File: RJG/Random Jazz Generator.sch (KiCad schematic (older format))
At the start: 19 parts, among them J101 EuroPower, J102 CV, J103 RND, J104 Gate, J105 Trig1, J106 Trig2, J107 Clock, J108 Trig3, J109 Trig4, U101 4520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

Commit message: Small improvements
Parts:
- added C101: 10u, symbol Device:CP
- added C102: 1u, symbol Device:CP
- added C103, C104: 100n, Capacitor_THT:C_Disc_D7.0mm_W2.5mm_P5.00mm, symbol Device:C
- renumbered U102 to U101, U101 to U102
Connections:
- net +12V: now also C101.1
- net +5V: now also C102.1, C103.2, C104.2
- net GND: now also C101.2, C102.2, C103.1, C104.1
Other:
- moved on the sheet: U101, U102C

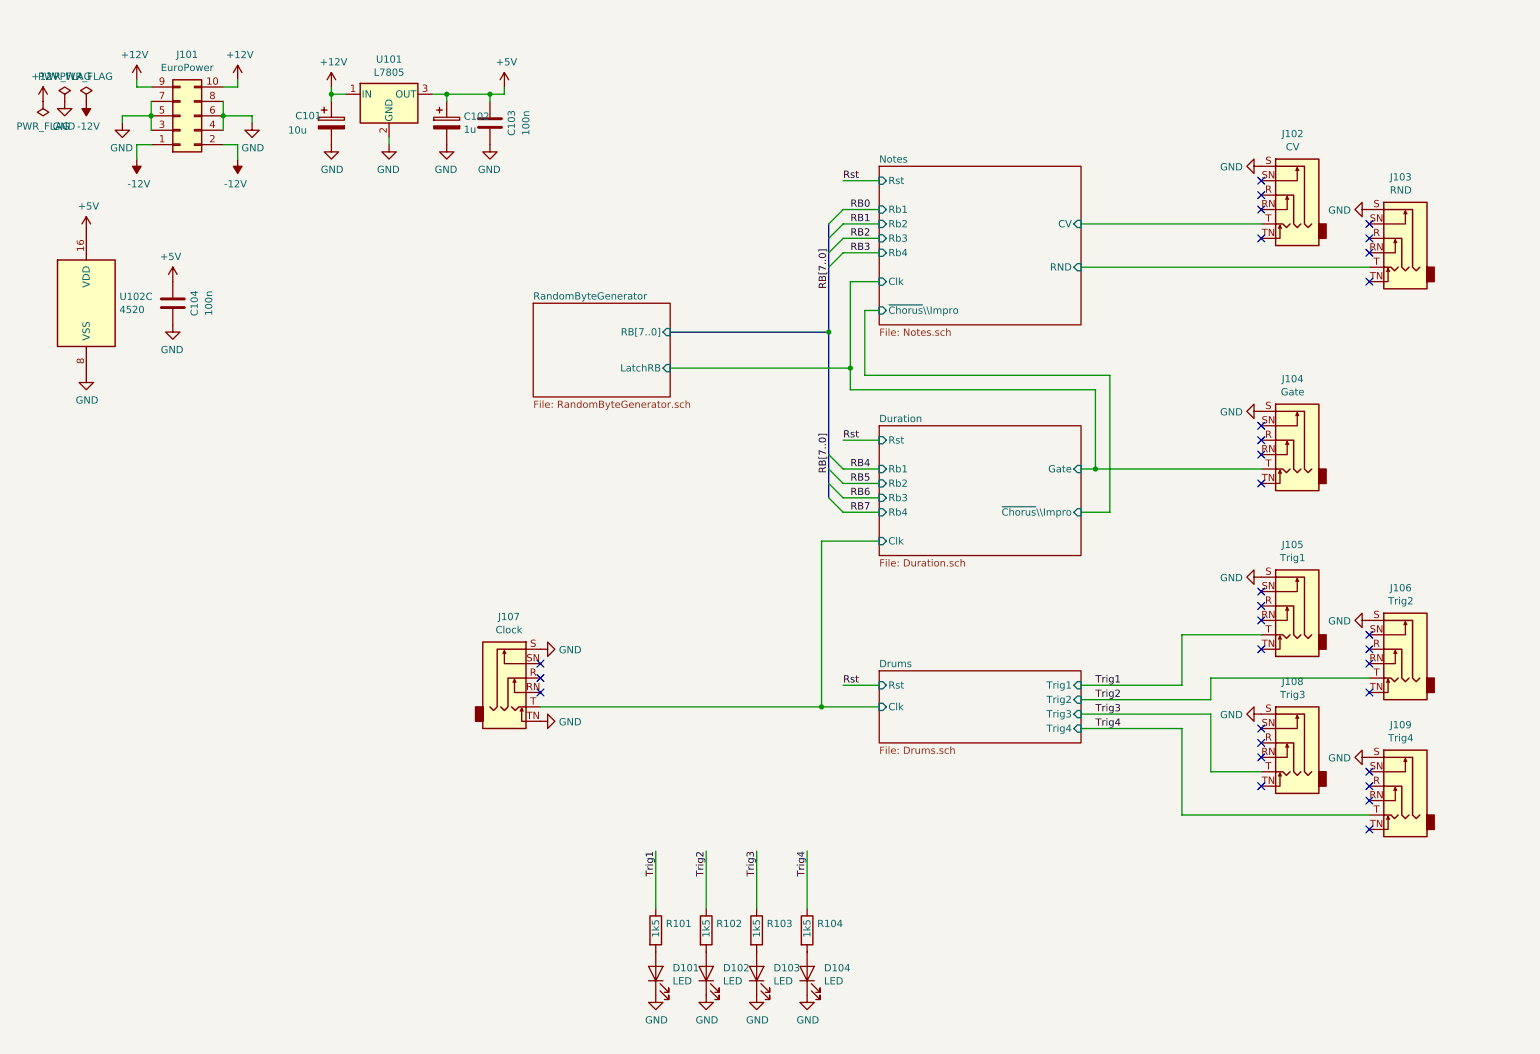
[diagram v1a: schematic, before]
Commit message: Schematic done
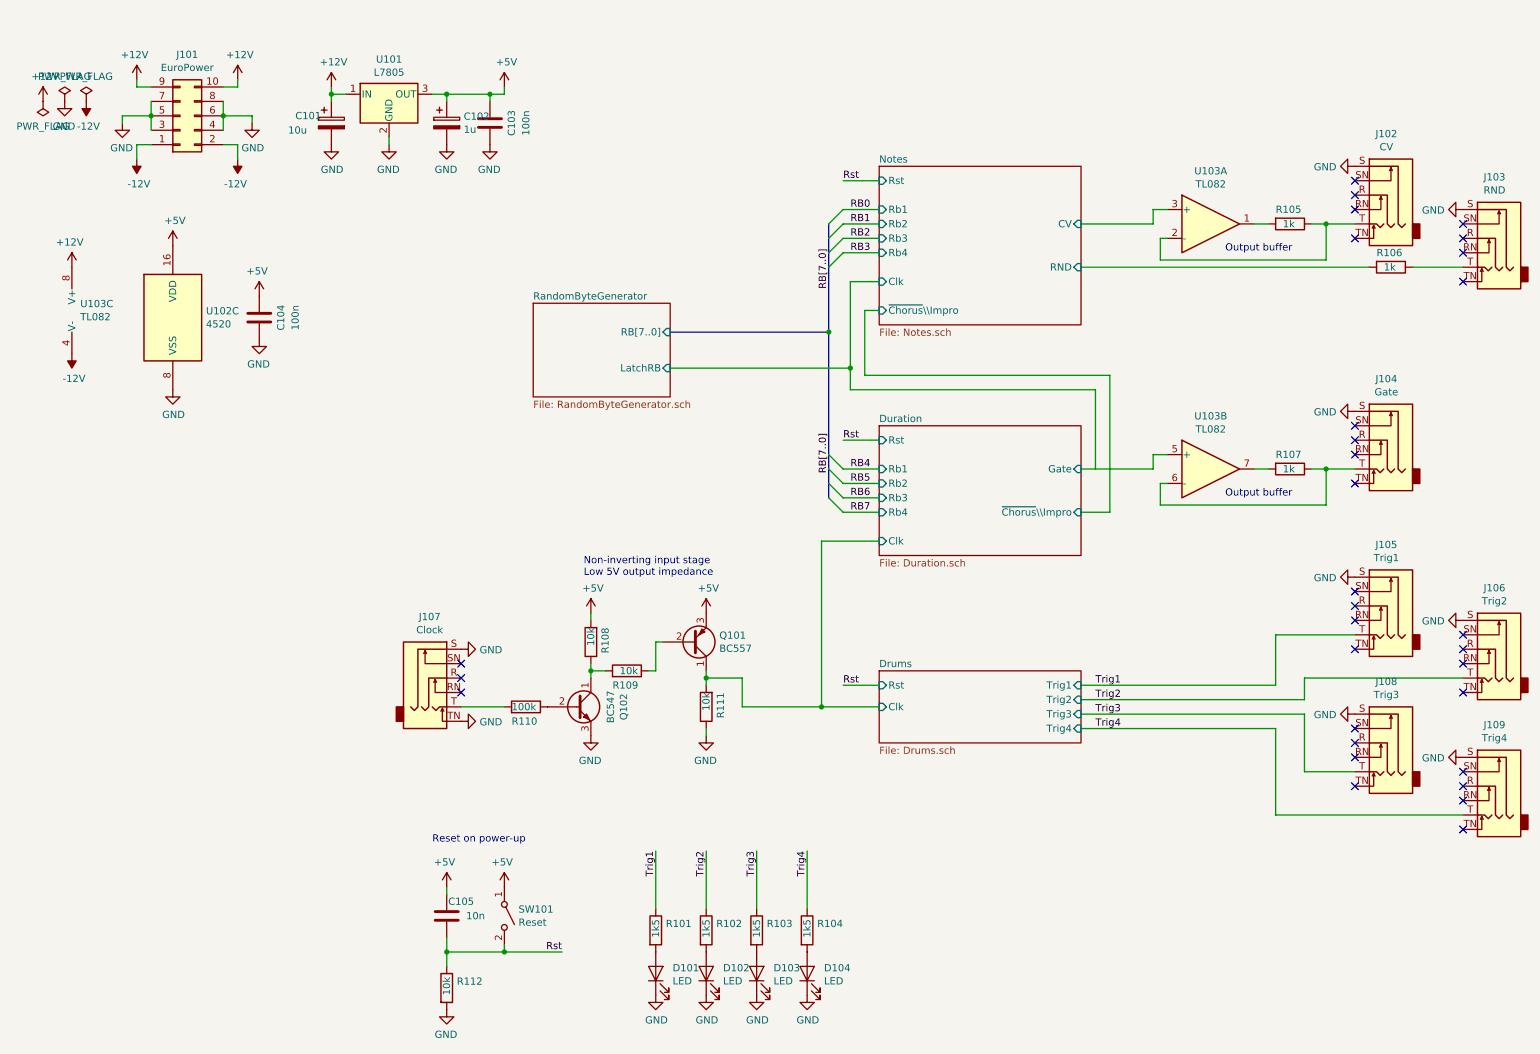
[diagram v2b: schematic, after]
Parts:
- added C105: 10n, Capacitor_THT:C_Disc_D7.0mm_W2.5mm_P5.00mm, symbol Device:C
- added Q101: BC557, Package_TO_SOT_THT:TO-92_Inline_Wide, symbol Transistor_BJT:BC557
- added Q102: BC547, Package_TO_SOT_THT:TO-92_Inline_Wide, symbol Transistor_BJT:BC547
- added R105, R106, R107: 1k, Resistor_THT:R_Axial_DIN0204_L3.6mm_D1.6mm_P7.62mm_Horizontal, symbol Device:R
- added R108, R109, R111, R112: 10k, Resistor_THT:R_Axial_DIN0204_L3.6mm_D1.6mm_P7.62mm_Horizontal, symbol Device:R
- added R110: 100k, Resistor_THT:R_Axial_DIN0204_L3.6mm_D1.6mm_P7.62mm_Horizontal, symbol Device:R
- added SW101: Reset, Button_Switch_THT:SW_PUSH_6mm, symbol Switch:SW_SPST
- added U103: TL082, Package_DIP:DIP-8_W7.62mm_LongPads, symbol Amplifier_Operational:TL082
- C101, C102: footprint (none) -> Capacitor_THT:CP_Radial_D8.0mm_P3.80mm
- U101: footprint (none) -> Package_TO_SOT_THT:TO-220-3_Vertical
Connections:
- net +12V: now also U103.8 (V+)
- net +5V: now also C105.2, Q101.3 (E), R108.2, SW101.1 (A)
- net -12V: now also U103.4 (V-)
- net Drums/Clk: now also Q101.1 (C), R111.2; no longer J107.T
- net Duration/Gate: now also U103.5 (+); no longer J104.T
- net GND: now also Q102.3 (E), R111.1, R112.2
- net Notes/CV: now also U103.3 (+); no longer J102.T
- net Notes/RND: now also R106.2; no longer J103.T
- net Rst: now also C105.1, R112.1, SW101.2 (B)
- new net: J107.T, R110.2
- new net: J104.T, R107.1, U103.6 (-)
- new net: J102.T, R105.1, U103.2 (-)
- new net: J103.T, R106.1
- new net: R105.2, U103.1
- new net: R107.2, U103.7
- new net: Q102.2 (B), R110.1
- new net: Q102.1 (C), R108.1, R109.2
- new net: Q101.2 (B), R109.1
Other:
- note added: "Non-inverting input stage\nLow 5V output impedance"
- note added: "Output buffer"
- note added: "Reset on power-up"
- moved on the sheet: C104, J102, J103, J104, J105, J106, J107, J108, J109, U102C

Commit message: First layout fit
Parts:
- removed D101, D102, D103, D104: LED, LED_THT:LED_D3.0mm, symbol Device:LED
- removed J101: EuroPower, Connector_IDC:IDC-Header_2x05_P2.54mm_Vertical, symbol Connector_Generic:Conn_02x05_Odd_Even
- removed R101, R102, R103, R104: 1k5, Resistor_THT:R_Axial_DIN0204_L3.6mm_D1.6mm_P7.62mm_Horizontal, symbol Device:R
- added H101, H102, H103: Mounting_Holes, Kosmo_panel:Kosmo_Panel_Dual_Mounting_Holes, symbol Kosmo:Mounting_Holes
- added J101: EuroPower, telec:EuroPower, symbol Connector:Screw_Terminal_01x03
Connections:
- net +12V: now also J101.3 (Pin_3)
- net -12V: now also J101.1 (Pin_1)
- net GND: now also H101.1, H102.1, H103.1, J101.2 (Pin_2)
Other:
- moved on the sheet: C105, R112, SW101

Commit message: Layout improvment
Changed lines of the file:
@@
 	6100 2050 6200 1950
 Wire Wire Line
-	6450 1950 6200 1950
-Text Label 6250 1950 0    50   ~ 0
+	6450 3750 6200 3750
+Text Label 6250 3750 0    50   ~ 0
 RB0
 Entry Wire Line
 	6100 2150 6200 2050
 Wire Wire Line
-	6450 2050 6200 2050
-Text Label 6250 2050 0    50   ~ 0
+	6450 3850 6200 3850
+Text Label 6250 3850 0    50   ~ 0
 RB1
 Entry Wire Line
 	6100 2250 6200 2150
 Wire Wire Line
-	6450 2150 6200 2150
-Text Label 6250 2150 0    50   ~ 0
+	6450 3950 6200 3950
+Text Label 6250 3950 0    50   ~ 0
 RB2
 Entry Wire Line
 	6100 2350 6200 2250
 Wire Wire Line
-	6450 2250 6200 2250
-Text Label 6250 2250 0    50   ~ 0
+	6450 4050 6200 4050
+Text Label 6250 4050 0    50   ~ 0
 RB3
 Wire Bus Line
@@
 	6100 3950 6200 4050
 Wire Wire Line
-	6450 4050 6200 4050
-Text Label 6250 4050 0    50   ~ 0
+	6450 2250 6200 2250
+Text Label 6250 1950 0    50   ~ 0
 RB7
 Entry Wire Line
 	6100 3850 6200 3950
 Wire Wire Line
-	6450 3950 6200 3950
-Text Label 6250 3950 0    50   ~ 0
+	6450 2150 6200 2150
+Text Label 6250 2050 0    50   ~ 0
 RB6
 Entry Wire Line
 	6100 3750 6200 3850
 Wire Wire Line
-	6450 3850 6200 3850
-Text Label 6250 3850 0    50   ~ 0
+	6450 2050 6200 2050
+Text Label 6250 2150 0    50   ~ 0
 RB5
 Entry Wire Line
 	6100 3650 6200 3750
 Wire Wire Line
-	6450 3750 6200 3750
-Text Label 6250 3750 0    50   ~ 0
+	6450 1950 6200 1950
+Text Label 6250 2250 0    50   ~ 0
 RB4
 Text Label 6100 3500 3    50   ~ 0
@@
 Text Notes 8850 3950 0    50   ~ 0
 Output buffer
-Wire Wire Line
-	7850 3750 8350 3750
 $Comp
 L power:GND #PWR0135
@@
 	-1   0    0    -1
 $EndComp
+Wire Wire Line
+	7850 3750 7950 3750
+Wire Wire Line
+	7950 3750 8350 3750
+Connection ~ 7950 3750
 Wire Bus Line
 	6100 2050 6100 2800

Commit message: Finsihed layout
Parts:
- added C106, C107: 100n, Capacitor_THT:C_Disc_D7.0mm_W2.5mm_P5.00mm, symbol Device:C
- U101: footprint Package_TO_SOT_THT:TO-220-3_Vertical -> Package_TO_SOT_THT:TO-220-3_Horizontal_TabDown
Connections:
- net +12V: now also C106.2
- net -12V: now also C107.2
- net Duration/Gate: now also U103.3 (+); no longer U103.5 (+)
- net GND: now also C106.1, C107.1
- net Notes/CV: now also U103.5 (+); no longer U103.3 (+)
- net at J104.T, R107.1: now also U103.2 (-); no longer U103.6 (-)
- net at J102.T, R105.1: now also U103.6 (-); no longer U103.2 (-)
- net at R105.2: now also U103.7; no longer U103.1
- net at R107.2: now also U103.1; no longer U103.7
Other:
- moved on the sheet: U103A, U103B
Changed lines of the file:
@@
 F 0 "U101" H 3050 1392 50  0000 C CNN
 F 1 "L7805" H 3050 1301 50  0000 C CNN
-F 2 "Package_TO_SOT_THT:TO-220-3_Vertical" H 3075 1000 50  0001 L CIN
+F 2 "Package_TO_SOT_THT:TO-220-3_Horizontal_TabDown" H 3075 1000 50  0001 L CIN
 F 3 "http://www.st.com/content/ccc/resource/technical/document/datasheet/41/4f/b3/b0/12/d4/47/88/CD00000444.pdf/files/CD00000444.pdf/jcr:content/translations/en.CD00000444.pdf" H 3050 1100 50  0001 C CNN
 	1    3050 1150
@@
 L Amplifier_Operational:TL082 U103
 U 1 1 6038C1EA
-P 8750 2050
-F 0 "U103" H 8750 2417 50  0000 C CNN
-F 1 "TL082" H 8750 2326 50  0000 C CNN
-F 2 "Package_DIP:DIP-8_W7.62mm_LongPads" H 8750 2050 50  0001 C CNN
-F 3 "http://www.ti.com/lit/ds/symlink/tl081.pdf" H 8750 2050 50  0001 C CNN
-	1    8750 2050
+P 8750 3750
+F 0 "U103" H 8750 4117 50  0000 C CNN
+F 1 "TL082" H 8750 4026 50  0000 C CNN
+F 2 "Package_DIP:DIP-8_W7.62mm_LongPads" H 8750 3750 50  0001 C CNN
+F 3 "http://www.ti.com/lit/ds/symlink/tl081.pdf" H 8750 3750 50  0001 C CNN
+	1    8750 3750
 	1    0    0    -1
 $EndComp
@@
 L Amplifier_Operational:TL082 U103
 U 2 1 603AFABE
-P 8750 3750
-F 0 "U103" H 8750 4117 50  0000 C CNN
-F 1 "TL082" H 8750 4026 50  0000 C CNN
-F 2 "Package_DIP:DIP-8_W7.62mm_LongPads" H 8750 3750 50  0001 C CNN
-F 3 "http://www.ti.com/lit/ds/symlink/tl081.pdf" H 8750 3750 50  0001 C CNN
-	2    8750 3750
+P 8750 2050
+F 0 "U103" H 8750 2417 50  0000 C CNN
+F 1 "TL082" H 8750 2326 50  0000 C CNN
+F 2 "Package_DIP:DIP-8_W7.62mm_LongPads" H 8750 2050 50  0001 C CNN
+F 3 "http://www.ti.com/lit/ds/symlink/tl081.pdf" H 8750 2050 50  0001 C CNN
+	2    8750 2050
 	1    0    0    -1
 $EndComp
@@
 	7950 3750 8350 3750
 Connection ~ 7950 3750
+$Comp
+L Device:C C106
+U 1 1 60C2F6BD
+P 2550 2700
+AR Path="/60C2F6BD" Ref="C106"  Part="1"
+AR Path="/5F345A0C/60C2F6BD" Ref="C?"  Part="1"
+F 0 "C106" V 2700 2700 50  0000 C CNN
+F 1 "100n" V 2800 2700 50  0000 C CNN
+F 2 "Capacitor_THT:C_Disc_D7.0mm_W2.5mm_P5.00mm" H 2588 2550 50  0001 C CNN
+F 3 "~" H 2550 2700 50  0001 C CNN
+	1    2550 2700
+	1    0    0    1
+$EndComp
+$Comp
+L power:GND #PWR0129
+U 1 1 60C2F6C3
+P 2550 2850
+AR Path="/60C2F6C3" Ref="#PWR0129"  Part="1"
+AR Path="/5F345A0C/60C2F6C3" Ref="#PWR?"  Part="1"
+F 0 "#PWR0129" H 2550 2600 50  0001 C CNN
+F 1 "GND" H 2555 2677 50  0000 C CNN
+F 2 "" H 2550 2850 50  0001 C CNN
+F 3 "" H 2550 2850 50  0001 C CNN
+	1    2550 2850
+	-1   0    0    -1
+$EndComp
+$Comp
+L Device:C C107
+U 1 1 60C32A60
+P 2950 2700
+AR Path="/60C32A60" Ref="C107"  Part="1"
+AR Path="/5F345A0C/60C32A60" Ref="C?"  Part="1"
+F 0 "C107" V 3100 2700 50  0000 C CNN
+F 1 "100n" V 3200 2700 50  0000 C CNN
+F 2 "Capacitor_THT:C_Disc_D7.0mm_W2.5mm_P5.00mm" H 2988 2550 50  0001 C CNN
+F 3 "~" H 2950 2700 50  0001 C CNN
+	1    2950 2700
+	1    0    0    1
+$EndComp
+$Comp
+L power:GND #PWR0130
+U 1 1 60C32A66
+P 2950 2850
+AR Path="/60C32A66" Ref="#PWR0130"  Part="1"
+AR Path="/5F345A0C/60C32A66" Ref="#PWR?"  Part="1"
+F 0 "#PWR0130" H 2950 2600 50  0001 C CNN
+F 1 "GND" H 2955 2677 50  0000 C CNN
+F 2 "" H 2950 2850 50  0001 C CNN
+F 3 "" H 2950 2850 50  0001 C CNN
+	1    2950 2850
+	-1   0    0    -1
+$EndComp
 Wire Bus Line
 	6100 2050 6100 2800
 Wire Bus Line
 	6100 2800 6100 3950
+$Comp
+L power:+12V #PWR0127
+U 1 1 60C35CE7
+P 2550 2550
+F 0 "#PWR0127" H 2550 2400 50  0001 C CNN
+F 1 "+12V" H 2565 2723 50  0000 C CNN
+F 2 "" H 2550 2550 50  0001 C CNN
+F 3 "" H 2550 2550 50  0001 C CNN
+	1    2550 2550
+	-1   0    0    -1
+$EndComp
+$Comp
+L power:-12V #PWR0128
+U 1 1 60C36318
+P 2950 2550
+F 0 "#PWR0128" H 2950 2650 50  0001 C CNN
+F 1 "-12V" H 2965 2723 50  0000 C CNN
+F 2 "" H 2950 2550 50  0001 C CNN
+F 3 "" H 2950 2550 50  0001 C CNN
+	1    2950 2550
+	-1   0    0    -1
+$EndComp
 $EndSCHEMATC

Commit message: Cleaner schematic, Better Layout
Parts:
- added D101: LED, LED_SMD:LED_1206_3216Metric_ReverseMount_Hole1.8x2.4mm, symbol Device:LED
- added LOGO1: telec, logo:telec-32, symbol Graphic:Logo_Open_Hardware_Small
- added R101: 1k, Resistor_SMD:R_1206_3216Metric_Pad1.42x1.75mm_HandSolder, symbol Device:R
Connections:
- net GND: now also D101.1 (K)
- net Drums/Clk renamed Clk
- net Clk: now also R101.1
- net Duration/Gate renamed Gate
- new net: D101.2 (A), R101.2
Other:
- moved on the sheet: C105, R112, SW101
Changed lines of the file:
@@
 Wire Wire Line
 	5500 5200 5500 5400
-Wire Wire Line
-	5500 5400 6050 5400
 Connection ~ 5250 5200
 Wire Wire Line
@@
 L Device:C C105
 U 1 1 6043816E
-P 5400 6650
+P 4950 6750
 AR Path="/6043816E" Ref="C105"  Part="1"
 AR Path="/5F345A0C/6043816E" Ref="C?"  Part="1"
-F 0 "C105" H 5500 6550 50  0000 C CNN
-F 1 "10n" H 5600 6650 50  0000 C CNN
-F 2 "Capacitor_THT:C_Disc_D7.0mm_W2.5mm_P5.00mm" H 5438 6500 50  0001 C CNN
-F 3 "~" H 5400 6650 50  0001 C CNN
-	1    5400 6650
+F 0 "C105" H 5050 6650 50  0000 C CNN
+F 1 "10n" H 5150 6750 50  0000 C CNN
+F 2 "Capacitor_THT:C_Disc_D7.0mm_W2.5mm_P5.00mm" H 4988 6600 50  0001 C CNN
+F 3 "~" H 4950 6750 50  0001 C CNN
+	1    4950 6750
 	1    0    0    1
 $EndComp
@@
 L power:GND #PWR0141
 U 1 1 60438174
-P 5400 7300
+P 4950 7400
 AR Path="/60438174" Ref="#PWR0141"  Part="1"
 AR Path="/5F345A0C/60438174" Ref="#PWR?"  Part="1"
-F 0 "#PWR0141" H 5400 7050 50  0001 C CNN
-F 1 "GND" H 5405 7127 50  0000 C CNN
-F 2 "" H 5400 7300 50  0001 C CNN
-F 3 "" H 5400 7300 50  0001 C CNN
-	1    5400 7300
+F 0 "#PWR0141" H 4950 7150 50  0001 C CNN
+F 1 "GND" H 4955 7227 50  0000 C CNN
+F 2 "" H 4950 7400 50  0001 C CNN
+F 3 "" H 4950 7400 50  0001 C CNN
+	1    4950 7400
 	-1   0    0    -1
 $EndComp
@@
 L power:+5V #PWR?
 U 1 1 6043817A
-P 5400 6450
+P 4950 6550
 AR Path="/5F345A0C/6043817A" Ref="#PWR?"  Part="1"
 AR Path="/6043817A" Ref="#PWR0139"  Part="1"
-F 0 "#PWR0139" H 5400 6300 50  0001 C CNN
-F 1 "+5V" H 5415 6623 50  0000 C CNN
-F 2 "" H 5400 6450 50  0001 C CNN
-F 3 "" H 5400 6450 50  0001 C CNN
-	1    5400 6450
+F 0 "#PWR0139" H 4950 6400 50  0001 C CNN
+F 1 "+5V" H 4965 6723 50  0000 C CNN
+F 2 "" H 4950 6550 50  0001 C CNN
+F 3 "" H 4950 6550 50  0001 C CNN
+	1    4950 6550
 	-1   0    0    -1
 $EndComp
@@
 L Device:R R112
 U 1 1 6043F27A
-P 5400 7150
-F 0 "R112" H 5470 7196 50  0000 L CNN
-F 1 "10k" V 5400 7100 50  0000 L CNN
-F 2 "Resistor_THT:R_Axial_DIN0204_L3.6mm_D1.6mm_P7.62mm_Horizontal" V 5330 7150 50  0001 C CNN
-F 3 "~" H 5400 7150 50  0001 C CNN
-	1    5400 7150
-	1    0    0    -1
-$EndComp
-Wire Wire Line
-	5400 6800 5400 6900
-Wire Wire Line
-	5400 6900 5800 6900
-Connection ~ 5400 6900
-Wire Wire Line
-	5400 6900 5400 7000
-Text Label 6200 6900 2    50   ~ 0
+P 4950 7250
+F 0 "R112" H 5020 7296 50  0000 L CNN
+F 1 "10k" V 4950 7200 50  0000 L CNN
+F 2 "Resistor_THT:R_Axial_DIN0204_L3.6mm_D1.6mm_P7.62mm_Horizontal" V 4880 7250 50  0001 C CNN
+F 3 "~" H 4950 7250 50  0001 C CNN
+	1    4950 7250
+	1    0    0    -1
+$EndComp
+Wire Wire Line
+	4950 6900 4950 7000
+Wire Wire Line
+	4950 7000 5350 7000
+Connection ~ 4950 7000
+Wire Wire Line
+	4950 7000 4950 7100
+Text Label 5750 7000 2    50   ~ 0
 Rst
 $Comp
 L Switch:SW_SPST SW?
 U 1 1 60455F05
-P 5800 6650
+P 5350 6750
 AR Path="/5F424A92/60455F05" Ref="SW?"  Part="1"
 AR Path="/5F425067/60455F05" Ref="SW?"  Part="1"
 AR Path="/60455F05" Ref="SW101"  Part="1"
-F 0 "SW101" V 5754 6748 50  0000 L CNN
-F 1 "Reset" V 5845 6748 50  0000 L CNN
-F 2 "Button_Switch_THT:SW_PUSH_6mm" H 5800 6650 50  0001 C CNN
-F 3 "~" H 5800 6650 50  0001 C CNN
-	1    5800 6650
+F 0 "SW101" V 5304 6848 50  0000 L CNN
+F 1 "Reset" V 5395 6848 50  0000 L CNN
+F 2 "Button_Switch_THT:SW_PUSH_6mm" H 5350 6750 50  0001 C CNN
+F 3 "~" H 5350 6750 50  0001 C CNN
+	1    5350 6750
 	0    1    1    0
 $EndComp
@@
 L power:+5V #PWR?
 U 1 1 60459007
-P 5800 6450
+P 5350 6550
 AR Path="/5F345A0C/60459007" Ref="#PWR?"  Part="1"
 AR Path="/60459007" Ref="#PWR0140"  Part="1"
-F 0 "#PWR0140" H 5800 6300 50  0001 C CNN
-F 1 "+5V" H 5815 6623 50  0000 C CNN
-F 2 "" H 5800 6450 50  0001 C CNN
-F 3 "" H 5800 6450 50  0001 C CNN
-	1    5800 6450
-	-1   0    0    -1
-$EndComp
-Wire Wire Line
-	5800 6850 5800 6900
-Connection ~ 5800 6900
-Wire Wire Line
-	5800 6900 6200 6900
-Wire Wire Line
-	5400 6500 5400 6450
-Text Notes 5300 6150 0    50   ~ 0
+F 0 "#PWR0140" H 5350 6400 50  0001 C CNN
+F 1 "+5V" H 5365 6723 50  0000 C CNN
+F 2 "" H 5350 6550 50  0001 C CNN
+F 3 "" H 5350 6550 50  0001 C CNN
+	1    5350 6550
+	-1   0    0    -1
+$EndComp
+Wire Wire Line
+	5350 6950 5350 7000
+Connection ~ 5350 7000
+Wire Wire Line
+	5350 7000 5750 7000
+Wire Wire Line
+	4950 6600 4950 6550
+Text Notes 4850 6250 0    50   ~ 0
 Reset on power-up
 $Comp
@@
 	-1   0    0    -1
 $EndComp
-Wire Bus Line
-	6100 2050 6100 2800
-Wire Bus Line
-	6100 2800 6100 3950
 $Comp
 L power:+12V #PWR0127
@@
 	-1   0    0    -1
 $EndComp
+$Comp
+L Device:LED D101
+U 1 1 60C6FA41
+P 6450 7200
+AR Path="/60C6FA41" Ref="D101"  Part="1"
+AR Path="/5F42563C/60C6FA41" Ref="D?"  Part="1"
+F 0 "D101" V 6489 7083 50  0000 R CNN
+F 1 "LED" V 6398 7083 50  0000 R CNN
+F 2 "LED_SMD:LED_1206_3216Metric_ReverseMount_Hole1.8x2.4mm" H 6450 7200 50  0001 C CNN
+F 3 "~" H 6450 7200 50  0001 C CNN
+	1    6450 7200
+	0    -1   -1   0
+$EndComp
+$Comp
+L power:GND #PWR0142
+U 1 1 60C6FA47
+P 6450 7350
+AR Path="/60C6FA47" Ref="#PWR0142"  Part="1"
+AR Path="/5F42563C/60C6FA47" Ref="#PWR?"  Part="1"
+F 0 "#PWR0142" H 6450 7100 50  0001 C CNN
+F 1 "GND" H 6455 7177 50  0000 C CNN
+F 2 "" H 6450 7350 50  0001 C CNN
+F 3 "" H 6450 7350 50  0001 C CNN
+	1    6450 7350
+	1    0    0    -1
+$EndComp
+$Comp
+L Device:R R101
+U 1 1 60C6FA4D
+P 6450 6900
+AR Path="/60C6FA4D" Ref="R101"  Part="1"
+AR Path="/5F42563C/60C6FA4D" Ref="R?"  Part="1"
+F 0 "R101" H 6520 6946 50  0000 L CNN
+F 1 "1k" V 6450 6850 50  0000 L CNN
+F 2 "Resistor_SMD:R_1206_3216Metric_Pad1.42x1.75mm_HandSolder" V 6380 6900 50  0001 C CNN
+F 3 "~" H 6450 6900 50  0001 C CNN
+	1    6450 6900
+	1    0    0    -1
+$EndComp
+Wire Wire Line
+	6450 6550 6450 6750
+Text Label 5500 5200 2    50   ~ 0
+Clk
+Text Label 6050 4250 0    50   ~ 0
+Clk
+Text Label 6100 5400 0    50   ~ 0
+Clk
+Wire Wire Line
+	5500 5400 6050 5400
+Text Label 6450 6550 3    50   ~ 0
+Clk
+Wire Bus Line
+	6100 2050 6100 2800
+Wire Bus Line
+	6100 2800 6100 3950
+Text Label 8250 3750 2    50   ~ 0
+Gate
+Text Label 6250 2450 0    50   ~ 0
+Gate
+Text Label 5250 3050 2    50   ~ 0
+Gate
+$Comp
+L Graphic:Logo_Open_Hardware_Small LOGO1
+U 1 1 60E67084
+P 2750 6950
+F 0 "LOGO1" H 2750 7225 50  0001 C CNN
+F 1 "telec" H 2750 6725 50  0001 C CNN
+F 2 "logo:telec-32" H 2750 6950 50  0001 C CNN
+F 3 "~" H 2750 6950 50  0001 C CNN
+	1    2750 6950
+	1    0    0    -1
+$EndComp
 $EndSCHEMATC
